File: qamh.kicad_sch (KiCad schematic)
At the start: 20 parts, among them J1 Eurorack_Power_16pin_Shrouded, J2 OUTPUT, J3 INPUT 1, J4 INPUT 2, J5 INPUT 3, J6 Conn_01x02_Pin, SW1 SW_Push

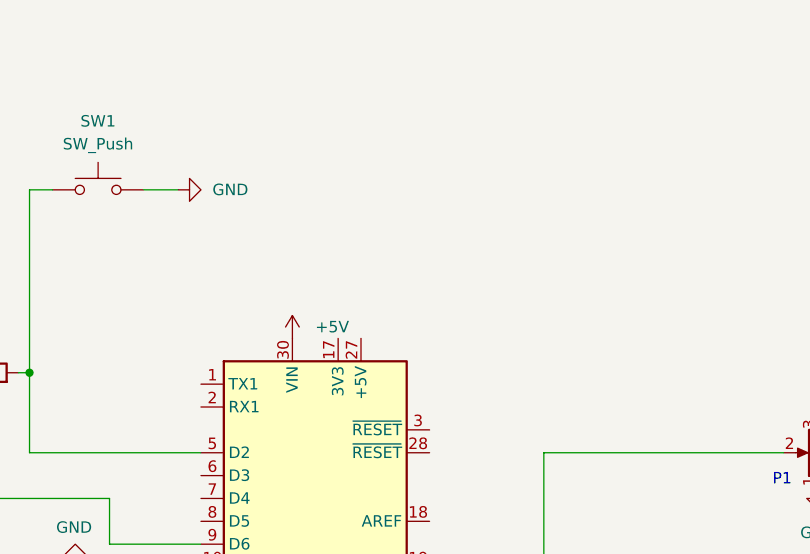
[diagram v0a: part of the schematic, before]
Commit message: header for plug/unplug 5V
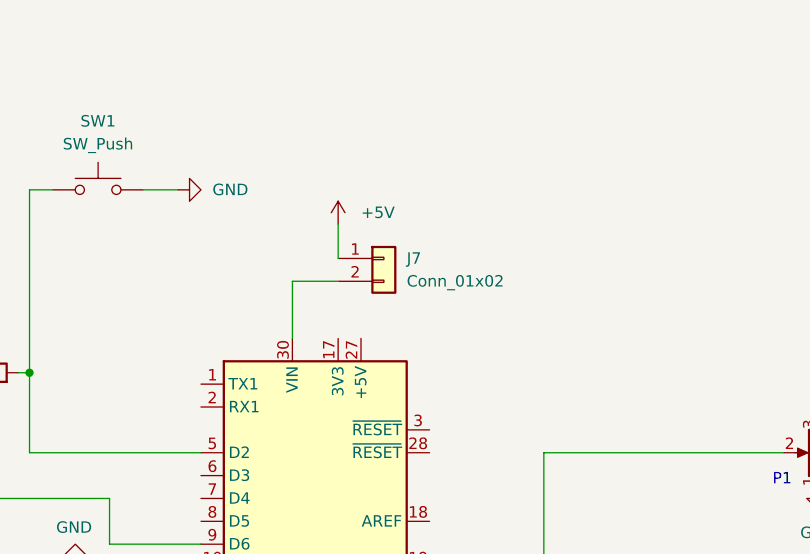
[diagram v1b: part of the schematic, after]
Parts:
- added J7: Conn_01x02, Connector_PinHeader_2.54mm:PinHeader_1x02_P2.54mm_Vertical, symbol 4ms_Connector:Conn_01x02
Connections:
- net +5V: now also J7.1 (Pin_1); no longer A1.30 (VIN)
- new net: A1.30 (VIN), J7.2 (Pin_2)
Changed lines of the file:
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@@
+    (stroke (width 0) (type default))
+  )
+  (wire (pts (xy 146.05 41.91) (xy 146.05 45.72))
+    (stroke (width 0) (type default))
+  )
+  (wire (pts (xy 140.97 54.61) (xy 140.97 48.26))
     (stroke (width 0) (type default))
   )
@@
   )
   (wire (pts (xy 160.02 87.63) (xy 156.21 87.63))
+    (stroke (width 0) (type default))
+  )
+  (wire (pts (xy 140.97 48.26) (xy 146.05 48.26))
     (stroke (width 0) (type default))
   )
@@
     )
   )
-  (symbol (lib_id "power:+5V") (at 140.97 54.61 0) (unit 1)
-    (in_bom yes) (on_board yes) (dnp no) (fields_autoplaced)
-    (property "Reference" "#PWR01" (at 140.97 58.42 0)
-      (effects (font (size 1.27 1.27)) hide)
-    )
-    (property "Value" "+5V" (at 143.51 53.3399 0)
-      (effects (font (size 1.27 1.27)) (justify left))
-    )
-    (property "Footprint" "" (at 140.97 54.61 0)
-      (effects (font (size 1.27 1.27)) hide)
-    )
-    (property "Datasheet" "" (at 140.97 54.61 0)
-      (effects (font (size 1.27 1.27)) hide)
-    )
-    (pin "1")
-    (instances
-      (project "qamh"
-        (path "/c13d4df3-e81e-4244-a624-8f3edbb92138"
-          (reference "#PWR01") (unit 1)
-        )
-      )
-    )
-  )
   (symbol (lib_id "power:GND") (at 199.39 105.41 0) (unit 1)
     (in_bom yes) (on_board yes) (dnp no) (fields_autoplaced)
@@
     )
   )
+  (symbol (lib_id "4ms_Connector:Conn_01x02") (at 151.13 45.72 0) (unit 1)
+    (in_bom yes) (on_board yes) (dnp no) (fields_autoplaced)
+    (property "Reference" "J7" (at 153.67 45.72 0)
+      (effects (font (size 1.27 1.27)) (justify left))
+    )
+    (property "Value" "Conn_01x02" (at 153.67 48.26 0)
+      (effects (font (size 1.27 1.27)) (justify left))
+    )
+    (property "Footprint" "Connector_PinHeader_2.54mm:PinHeader_1x02_P2.54mm_Vertical" (at 150.495 41.275 0)
+      (effects (font (size 1.27 1.27)) hide)
+    )
+    (property "Datasheet" "" (at 151.13 45.72 0)
+      (effects (font (size 1.27 1.27)) hide)
+    )
+    (property "Specifications" "Pins_01x02, Header, Male Pins, 1*2, spacing 2.54mm, straight pin" (at 148.59 53.594 0)
+      (effects (font (size 1.27 1.27)) (justify left) hide)
+    )
+    (property "Manufacturer" "TAD" (at 148.59 55.118 0)
+      (effects (font (size 1.27 1.27)) (justify left) hide)
+    )
+    (property "Part Number" "1-0201FBV0T" (at 148.59 56.642 0)
+      (effects (font (size 1.27 1.27)) (justify left) hide)
+    )
+    (property "Production Stage" "B" (at 151.13 45.72 0)
+      (effects (font (size 1.27 1.27)) hide)
+    )
+    (pin "1")
+    (pin "2")
+    (instances
+      (project "qamh"
+        (path "/c13d4df3-e81e-4244-a624-8f3edbb92138"
+          (reference "J7") (unit 1)
+        )
+      )
+    )
+  )
   (symbol (lib_id "Connector:AudioJack2") (at 243.84 83.82 180) (unit 1)
     (in_bom yes) (on_board yes) (dnp no) (fields_autoplaced)
@@
         )
       )
+    )
+  )
+  (symbol (lib_id "power:+5V") (at 146.05 41.91 0) (unit 1)
+    (in_bom yes) (on_board yes) (dnp no) (fields_autoplaced)
+    (property "Reference" "#PWR05" (at 146.05 45.72 0)
+      (effects (font (size 1.27 1.27)) hide)
+    )
+    (property "Value" "+5V" (at 148.59 40.6399 0)
+      (effects (font (size 1.27 1.27)) (justify left))
+    )
+    (property "Footprint" "" (at 146.05 41.91 0)
+      (effects (font (size 1.27 1.27)) hide)
+    )
+    (property "Datasheet" "" (at 146.05 41.91 0)
+      (effects (font (size 1.27 1.27)) hide)
+    )
+    (pin "1")
+    (instances
+      (project "qamh"
+        (path "/c13d4df3-e81e-4244-a624-8f3edbb92138"
+          (reference "#PWR05") (unit 1)
+        )
+      )
